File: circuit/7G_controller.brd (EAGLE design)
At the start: 63 x 69.5 mm, 22 parts, among them Q1 32768Hz, T1 TPS1101D

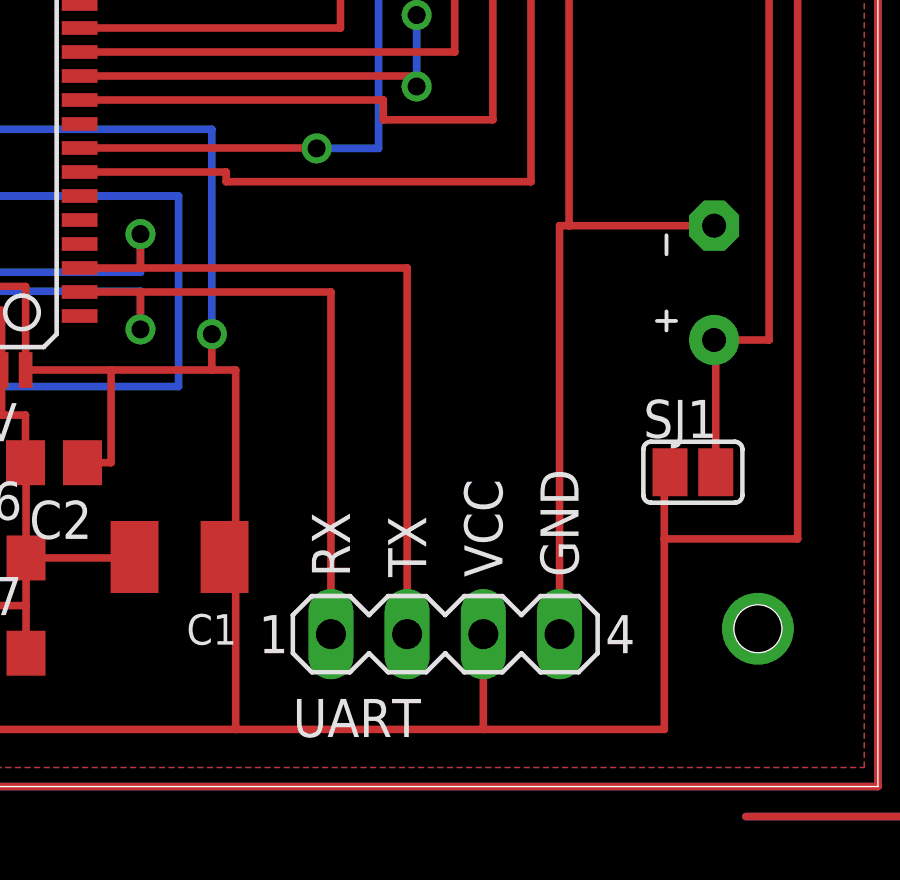
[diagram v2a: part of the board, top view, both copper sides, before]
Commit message: 
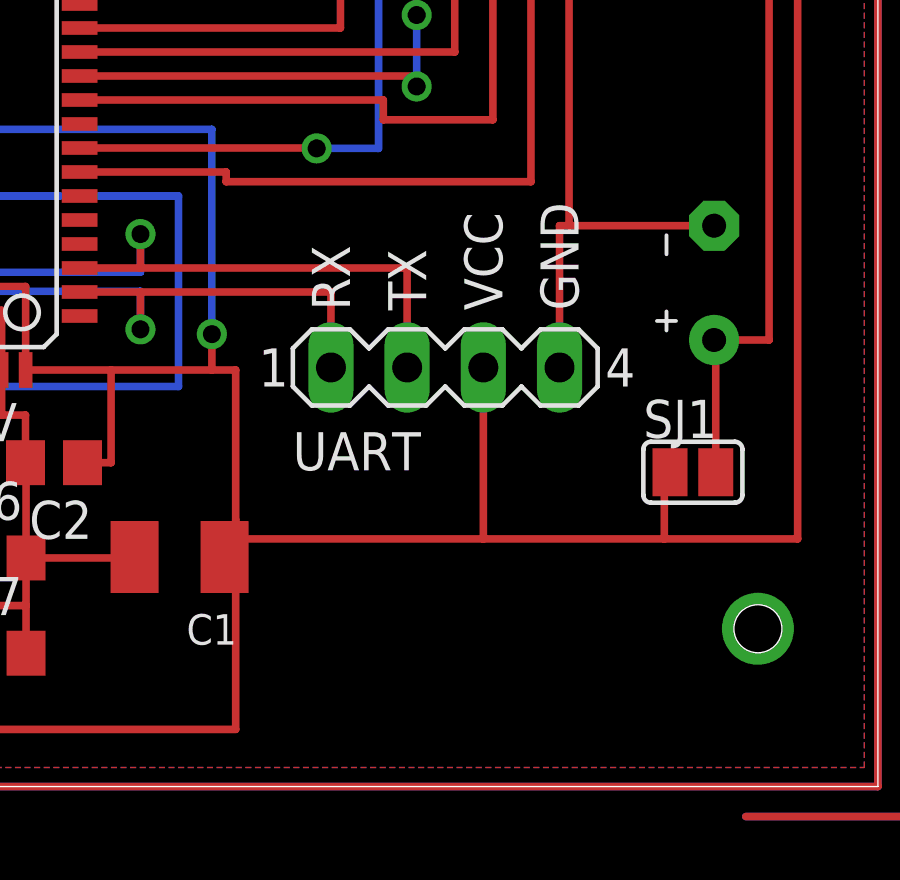
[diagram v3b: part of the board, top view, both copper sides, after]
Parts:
- moved UART 8.89 mm to (48.6, 16.5)
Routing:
- net N$29: track 101.7 -> 92.8 mm
- net N$30: track 111.5 -> 102.6 mm
- net GND: track 234.3 -> 225.4 mm
- net VCC: track 297.4 -> 293.6 mm
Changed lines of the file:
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@@
 <setting verticaltext="up"/>
 </settings>
-<grid distance="0.0125" unitdist="inch" unit="inch" style="lines" multiple="1" display="yes" altdistance="0.025" altunitdist="inch" altunit="inch"/>
+<grid distance="0.05" unitdist="inch" unit="mm" style="lines" multiple="1" display="yes" altdistance="0.025" altunitdist="inch" altunit="inch"/>
 <layers>
 <layer number="1" name="Top" color="4" fill="1" visible="yes" active="yes"/>
@@
 <layer number="17" name="Pads" color="2" fill="1" visible="yes" active="yes"/>
 <layer number="18" name="Vias" color="2" fill="1" visible="yes" active="yes"/>
-<layer number="19" name="Unrouted" color="6" fill="1" visible="no" active="yes"/>
-<layer number="20" name="Dimension" color="15" fill="1" visible="no" active="yes"/>
-<layer number="21" name="tPlace" color="7" fill="1" visible="no" active="yes"/>
-<layer number="22" name="bPlace" color="7" fill="1" visible="no" active="yes"/>
-<layer number="23" name="tOrigins" color="15" fill="1" visible="no" active="yes"/>
-<layer number="24" name="bOrigins" color="15" fill="1" visible="no" active="yes"/>
-<layer number="25" name="tNames" color="7" fill="1" visible="no" active="yes"/>
-<layer number="26" name="bNames" color="7" fill="1" visible="no" active="yes"/>
+<layer number="19" name="Unrouted" color="6" fill="1" visible="yes" active="yes"/>
+<layer number="20" name="Dimension" color="15" fill="1" visible="yes" active="yes"/>
+<layer number="21" name="tPlace" color="7" fill="1" visible="yes" active="yes"/>
+<layer number="22" name="bPlace" color="7" fill="1" visible="yes" active="yes"/>
+<layer number="23" name="tOrigins" color="15" fill="1" visible="yes" active="yes"/>
+<layer number="24" name="bOrigins" color="15" fill="1" visible="yes" active="yes"/>
+<layer number="25" name="tNames" color="7" fill="1" visible="yes" active="yes"/>
+<layer number="26" name="bNames" color="7" fill="1" visible="yes" active="yes"/>
 <layer number="27" name="tValues" color="7" fill="1" visible="no" active="yes"/>
 <layer number="28" name="bValues" color="7" fill="1" visible="no" active="yes"/>
@@
 <layer number="46" name="Milling" color="3" fill="1" visible="no" active="yes"/>
 <layer number="47" name="Measures" color="7" fill="1" visible="no" active="yes"/>
-<layer number="48" name="Document" color="7" fill="1" visible="no" active="yes"/>
+<layer number="48" name="Document" color="7" fill="1" visible="yes" active="yes"/>
 <layer number="49" name="Reference" color="7" fill="1" visible="no" active="yes"/>
 <layer number="50" name="dxf" color="7" fill="1" visible="no" active="no"/>
-<layer number="51" name="tDocu" color="7" fill="1" visible="no" active="yes"/>
-<layer number="52" name="bDocu" color="7" fill="1" visible="no" active="yes"/>
+<layer number="51" name="tDocu" color="7" fill="1" visible="yes" active="yes"/>
+<layer number="52" name="bDocu" color="7" fill="1" visible="yes" active="yes"/>
 <layer number="53" name="tGND_GNDA" color="7" fill="9" visible="no" active="no"/>
 <layer number="54" name="bGND_GNDA" color="1" fill="9" visible="no" active="no"/>
@@
 <element name="MTRX_CONN" library="KileParts" package="SS7G_CONN_SMD" value="SS7G_CONNSMD" x="17" y="44.5"/>
 <element name="BAT1" library="KileParts" package="BATTERY" value="" x="57.54" y="19.33" rot="R90"/>
-<element name="UART" library="KileParts" package="UART_PORT" value="" x="48.5775" y="7.62">
-<attribute name="OC_NEWARK" value="unknown" x="48.5775" y="7.62" size="1.778" layer="27" display="off"/>
-<attribute name="MPN" value="" x="48.5775" y="7.62" size="1.778" layer="27" display="off"/>
-<attribute name="MF" value="" x="48.5775" y="7.62" size="1.778" layer="27" display="off"/>
-<attribute name="OC_FARNELL" value="unknown" x="48.5775" y="7.62" size="1.778" layer="27" display="off"/>
+<element name="UART" library="KileParts" package="UART_PORT" value="" x="48.5775" y="16.51">
+<attribute name="OC_NEWARK" value="unknown" x="48.5775" y="16.51" size="1.778" layer="27" display="off"/>
+<attribute name="MPN" value="" x="48.5775" y="16.51" size="1.778" layer="27" display="off"/>
+<attribute name="MF" value="" x="48.5775" y="16.51" size="1.778" layer="27" display="off"/>
+<attribute name="OC_FARNELL" value="unknown" x="48.5775" y="16.51" size="1.778" layer="27" display="off"/>
 </element>
 <element name="C5" library="rcl" package="SMC_B" value="4.7uF" x="58.13125" y="43.5675" rot="R270"/>
@@
 <wire x1="10" y1="47.04" x2="10" y2="57.58375" width="0.254" layer="1"/>
 <wire x1="37.43875" y1="16.425" x2="34.59" y2="16.425" width="0.254" layer="1"/>
-<wire x1="55.88" y1="4.445" x2="49.8475" y2="4.445" width="0.254" layer="1"/>
-<wire x1="49.8475" y1="4.445" x2="49.8475" y2="7.62" width="0.254" layer="1"/>
+<wire x1="49.8475" y1="10.795" x2="49.8475" y2="16.51" width="0.254" layer="1"/>
 <wire x1="31.39" y1="32.025" x2="31.4325" y2="32.025" width="0.254" layer="1"/>
 <wire x1="31.4325" y1="32.025" x2="31.4325" y2="19.20875" width="0.254" layer="1"/>
@@
 <contactref element="SJ1" pad="1"/>
 <contactref element="C7" pad="1"/>
-<wire x1="49.8475" y1="4.445" x2="41.5925" y2="4.445" width="0.254" layer="1"/>
-<wire x1="41.5925" y1="16.425" x2="41.5925" y2="10.16" width="0.254" layer="1"/>
+<wire x1="41.5925" y1="16.425" x2="41.5925" y2="11.43" width="0.254" layer="1"/>
+<wire x1="41.5925" y1="10.795" x2="41.5925" y2="10.16" width="0.254" layer="1"/>
 <wire x1="41.5925" y1="10.16" x2="41.5925" y2="4.445" width="0.254" layer="1"/>
 <wire x1="41.2225" y1="10.19125" x2="40.9575" y2="10.19125" width="0.254" layer="1"/>
@@
 <wire x1="7.9375" y1="13.6525" x2="7.9375" y2="5.08" width="0.254" layer="1"/>
 <wire x1="7.9375" y1="5.08" x2="18.0975" y2="5.08" width="0.254" layer="1"/>
-<wire x1="55.88" y1="4.445" x2="55.88" y2="10.795" width="0.254" layer="1"/>
 <wire x1="55.88" y1="10.795" x2="55.88" y2="13.0175" width="0.254" layer="1"/>
 <wire x1="55.88" y1="13.0175" x2="56.0705" y2="13.0175" width="0.254" layer="1"/>
@@
 <wire x1="60.325" y1="37.465" x2="60.325" y2="10.795" width="0.254" layer="1"/>
 <wire x1="60.325" y1="10.795" x2="55.88" y2="10.795" width="0.254" layer="1"/>
+<wire x1="55.88" y1="10.795" x2="49.8475" y2="10.795" width="0.254" layer="1"/>
+<wire x1="49.8475" y1="10.795" x2="41.5925" y2="10.795" width="0.254" layer="1"/>
+<wire x1="41.5925" y1="10.795" x2="41.5925" y2="11.43" width="0.254" layer="1"/>
 </signal>
 <signal name="GND">
@@
 <wire x1="30.63875" y1="18.415" x2="25.79" y2="18.415" width="0.254" layer="1"/>
 <wire x1="25.79" y1="18.415" x2="25.79" y2="16.425" width="0.254" layer="1"/>
-<wire x1="52.3875" y1="7.62" x2="52.3875" y2="21.235" width="0.254" layer="1"/>
+<wire x1="52.3875" y1="16.51" x2="52.3875" y2="21.235" width="0.254" layer="1"/>
 <wire x1="57.54" y1="21.235" x2="52.705" y2="21.235" width="0.254" layer="1"/>
 <wire x1="52.705" y1="21.235" x2="52.3875" y2="21.235" width="0.254" layer="1"/>
@@
 <wire x1="36.39" y1="19.025" x2="38.4175" y2="19.025" width="0.254" layer="1"/>
 <wire x1="38.4175" y1="19.025" x2="44.7675" y2="19.025" width="0.254" layer="1"/>
-<wire x1="44.7675" y1="19.025" x2="44.7675" y2="7.62" width="0.254" layer="1"/>
+<wire x1="44.7675" y1="19.025" x2="44.7675" y2="16.51" width="0.254" layer="1"/>
 <contactref element="DBG_JACK" pad="4"/>
 <wire x1="22.225" y1="60.58" x2="23.8125" y2="60.58" width="0.254" layer="16"/>
@@
 <wire x1="36.39" y1="19.825" x2="38.4175" y2="19.825" width="0.254" layer="1"/>
 <wire x1="38.4175" y1="19.825" x2="47.3075" y2="19.825" width="0.254" layer="1"/>
-<wire x1="47.3075" y1="19.825" x2="47.3075" y2="7.62" width="0.254" layer="1"/>
+<wire x1="47.3075" y1="19.825" x2="47.3075" y2="16.51" width="0.254" layer="1"/>
 <contactref element="DBG_JACK" pad="2"/>
 <contactref element="DBG_JACK" pad="3"/>

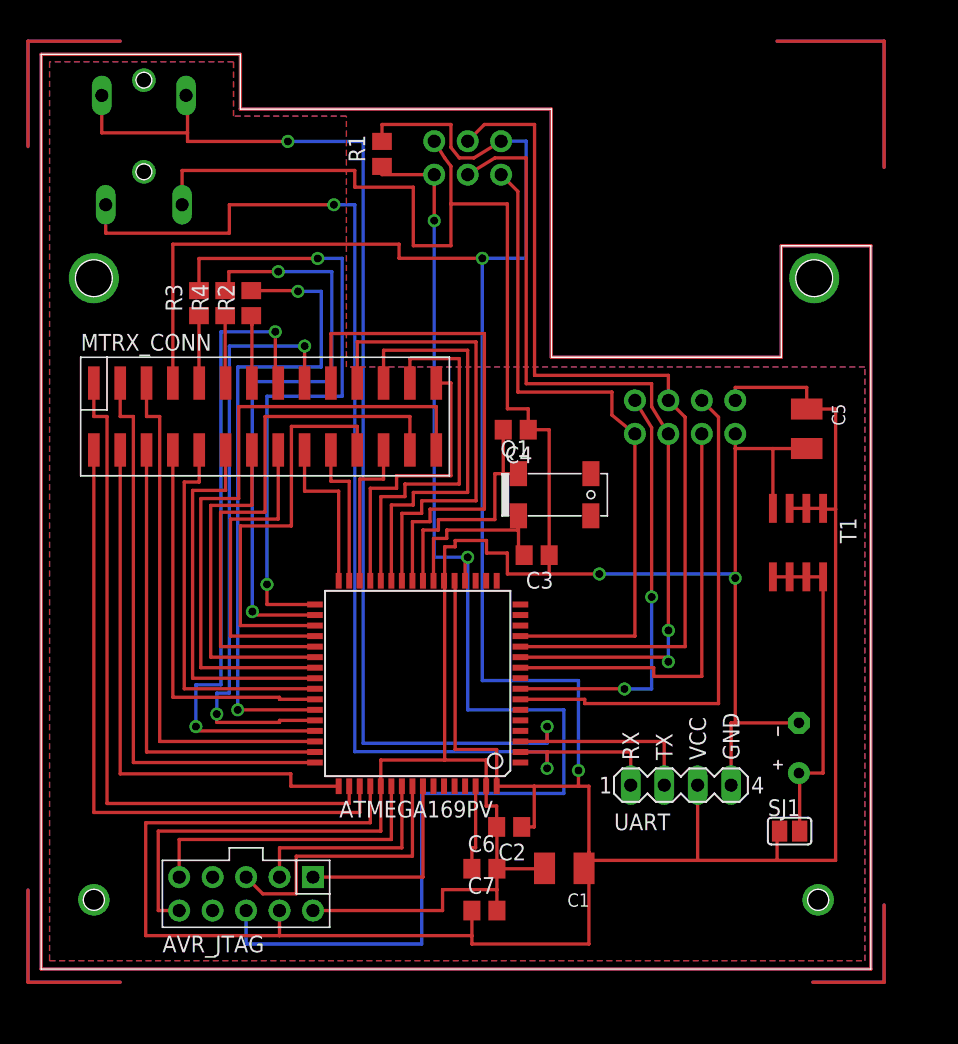
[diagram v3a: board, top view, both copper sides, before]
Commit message: 
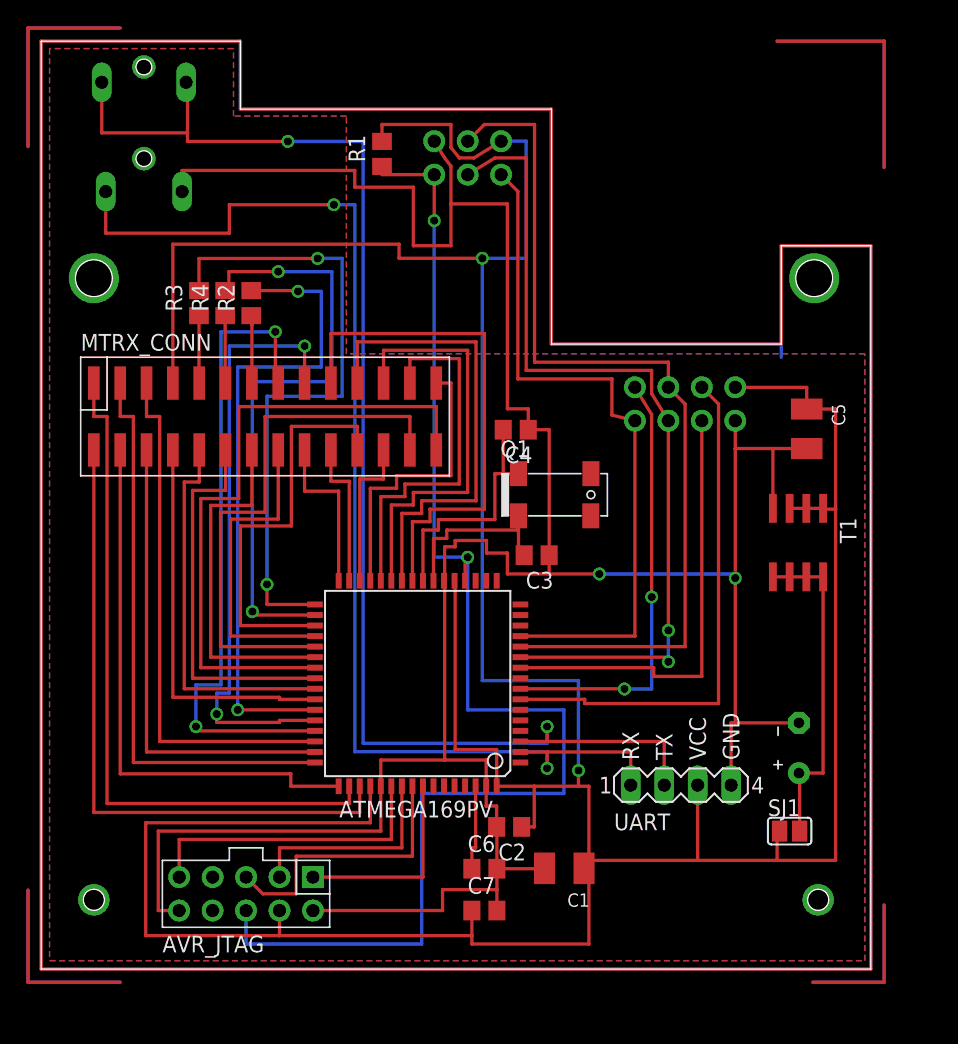
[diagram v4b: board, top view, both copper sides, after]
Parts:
- moved DBG_JACK 1.00 mm to (7.80, 69.6)
- moved NRF24L01 1.00 mm to (48.9, 45.5)
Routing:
- net N$30: track 102.6 -> 104.5 mm
- net N$1: track 281.8 -> 282.9 mm
- net N$3: track 15.0 -> 16.0 mm
- net N$29: track 92.8 -> 93.8 mm
- net N$13: track 15.0 -> 16.0 mm
- net IRQ: track 32.2 -> 33.2 mm
- net CSN: track 38.9 -> 39.9 mm
- net CE: track 32.8 -> 33.8 mm
- net VCC: track 293.6 -> 292.7 mm
- net MISO: track 52.2 -> 52.8 mm
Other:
- board size 63 x 69.5 mm -> 63 x 70.5 mm
